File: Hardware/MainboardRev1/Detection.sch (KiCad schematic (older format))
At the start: 16 parts, among them J10 Switch_3, J11 Switch_2, J12 Switch_4, J9 Switch_1

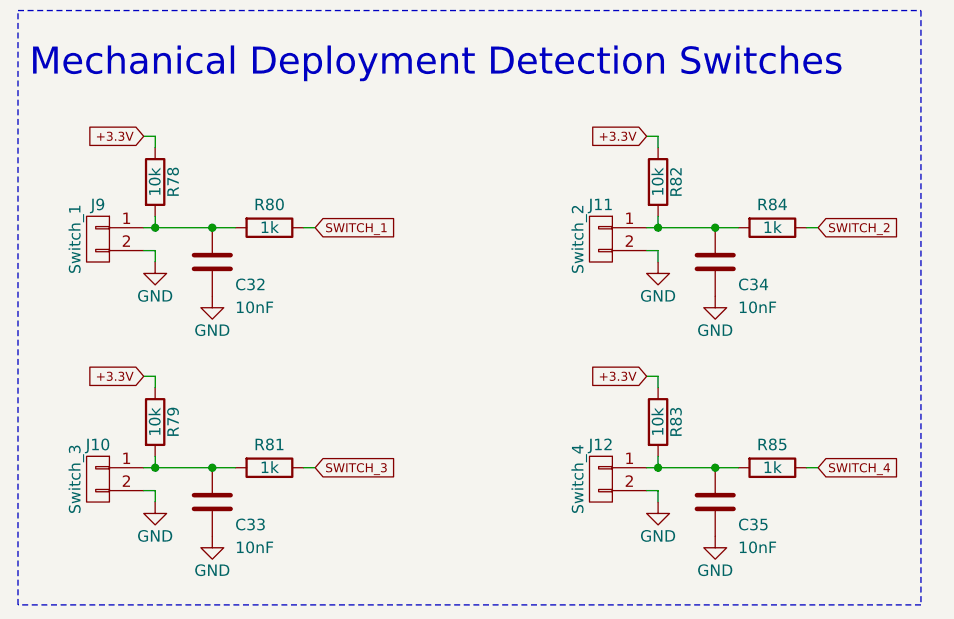
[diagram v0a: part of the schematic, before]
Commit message: Small changes to schematic: Added voltage dividers for analog inputs, small net changes. Added footprints for each part
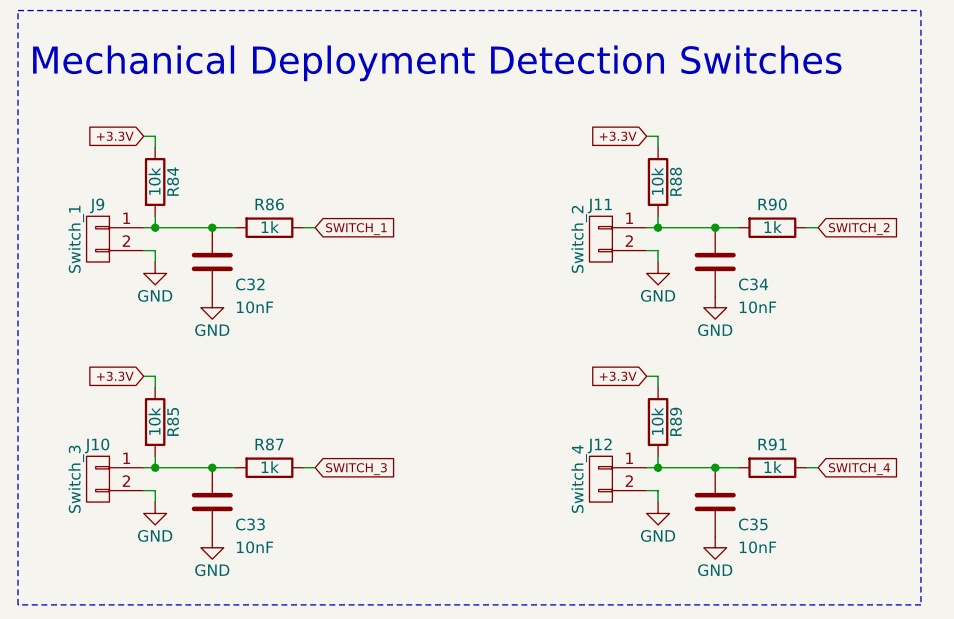
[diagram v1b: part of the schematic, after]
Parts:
- C32, C33, C34, C35: footprint (none) -> Capacitors_SMD:C_0603_HandSoldering
- J10, J11, J12, J9: footprint (none) -> Dans_Parts:Molex_Microfit3_Header_02x01_Straight
- R84: renamed from R78; footprint (none) -> Resistors_SMD:R_0603_HandSoldering
- R85: renamed from R79; footprint (none) -> Resistors_SMD:R_0603_HandSoldering
- R86: renamed from R80; footprint (none) -> Resistors_SMD:R_0603_HandSoldering
- R87: renamed from R81; footprint (none) -> Resistors_SMD:R_0603_HandSoldering
- R88: renamed from R82; footprint (none) -> Resistors_SMD:R_0603_HandSoldering
- R89: renamed from R83; footprint (none) -> Resistors_SMD:R_0603_HandSoldering
- R90: renamed from R84; footprint (none) -> Resistors_SMD:R_0603_HandSoldering
- R91: renamed from R85; footprint (none) -> Resistors_SMD:R_0603_HandSoldering
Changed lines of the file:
@@
 F 0 "J9" H 2150 2250 50  0000 C CNN
 F 1 "Switch_1" V 2250 2100 50  0000 C CNN
-F 2 "" H 2150 2100 50  0000 C CNN
+F 2 "Dans_Parts:Molex_Microfit3_Header_02x01_Straight" H 2150 2100 50  0001 C CNN
 F 3 "" H 2150 2100 50  0000 C CNN
 	1    2150 2100
@@
 $EndComp
 $Comp
-L GND #PWR070
+L GND #PWR072
 U 1 1 5AFB61FA
 P 2400 2200
-F 0 "#PWR070" H 2400 1950 50  0001 C CNN
+F 0 "#PWR072" H 2400 1950 50  0001 C CNN
 F 1 "GND" H 2400 2050 50  0000 C CNN
 F 2 "" H 2400 2200 50  0000 C CNN
@@
 	2400 2150 2350 2150
 $Comp
-L R R78
+L R R84
 U 1 1 5AFB6399
 P 2400 1850
-F 0 "R78" V 2480 1850 50  0000 C CNN
+F 0 "R84" V 2480 1850 50  0000 C CNN
 F 1 "10k" V 2400 1850 50  0000 C CNN
-F 2 "" V 2330 1850 50  0000 C CNN
+F 2 "Resistors_SMD:R_0603_HandSoldering" V 2330 1850 50  0001 C CNN
 F 3 "" H 2400 1850 50  0000 C CNN
 	1    2400 1850
@@
 F 0 "C32" H 2750 2100 50  0000 L CNN
 F 1 "10nF" H 2750 2000 50  0000 L CNN
-F 2 "" H 2688 2050 50  0000 C CNN
+F 2 "Capacitors_SMD:C_0603_HandSoldering" H 2688 2050 50  0001 C CNN
 F 3 "" H 2650 2200 50  0000 C CNN
 	1    2650 2200
@@
 	2350 2050 2750 2050
 $Comp
-L GND #PWR071
+L GND #PWR073
 U 1 1 5AFB65B1
 P 2650 2350
-F 0 "#PWR071" H 2650 2100 50  0001 C CNN
+F 0 "#PWR073" H 2650 2100 50  0001 C CNN
 F 1 "GND" H 2650 2200 50  0000 C CNN
 F 2 "" H 2650 2350 50  0000 C CNN
@@
 $EndComp
 $Comp
-L R R80
+L R R86
 U 1 1 5AFB65E3
 P 2900 2050
-F 0 "R80" V 2800 2050 50  0000 C CNN
+F 0 "R86" V 2800 2050 50  0000 C CNN
 F 1 "1k" V 2900 2050 50  0000 C CNN
-F 2 "" V 2830 2050 50  0000 C CNN
+F 2 "Resistors_SMD:R_0603_HandSoldering" V 2830 2050 50  0001 C CNN
 F 3 "" H 2900 2050 50  0000 C CNN
 	1    2900 2050
@@
 F 0 "J10" H 2150 3300 50  0000 C CNN
 F 1 "Switch_3" V 2250 3150 50  0000 C CNN
-F 2 "" H 2150 3150 50  0000 C CNN
+F 2 "Dans_Parts:Molex_Microfit3_Header_02x01_Straight" H 2150 3150 50  0001 C CNN
 F 3 "" H 2150 3150 50  0000 C CNN
 	1    2150 3150
@@
 $EndComp
 $Comp
-L GND #PWR072
+L GND #PWR074
 U 1 1 5AFB6AE1
 P 2400 3250
-F 0 "#PWR072" H 2400 3000 50  0001 C CNN
+F 0 "#PWR074" H 2400 3000 50  0001 C CNN
 F 1 "GND" H 2400 3100 50  0000 C CNN
 F 2 "" H 2400 3250 50  0000 C CNN
@@
 	2400 3200 2350 3200
 $Comp
-L R R79
+L R R85
 U 1 1 5AFB6AE9
 P 2400 2900
-F 0 "R79" V 2480 2900 50  0000 C CNN
+F 0 "R85" V 2480 2900 50  0000 C CNN
 F 1 "10k" V 2400 2900 50  0000 C CNN
-F 2 "" V 2330 2900 50  0000 C CNN
+F 2 "Resistors_SMD:R_0603_HandSoldering" V 2330 2900 50  0001 C CNN
 F 3 "" H 2400 2900 50  0000 C CNN
 	1    2400 2900
@@
 F 0 "C33" H 2750 3150 50  0000 L CNN
 F 1 "10nF" H 2750 3050 50  0000 L CNN
-F 2 "" H 2688 3100 50  0000 C CNN
+F 2 "Capacitors_SMD:C_0603_HandSoldering" H 2688 3100 50  0001 C CNN
 F 3 "" H 2650 3250 50  0000 C CNN
 	1    2650 3250
@@
 	2350 3100 2750 3100
 $Comp
-L GND #PWR073
+L GND #PWR075
 U 1 1 5AFB6AFB
 P 2650 3400
-F 0 "#PWR073" H 2650 3150 50  0001 C CNN
+F 0 "#PWR075" H 2650 3150 50  0001 C CNN
 F 1 "GND" H 2650 3250 50  0000 C CNN
 F 2 "" H 2650 3400 50  0000 C CNN
@@
 $EndComp
 $Comp
-L R R81
+L R R87
 U 1 1 5AFB6B01
 P 2900 3100
-F 0 "R81" V 2800 3100 50  0000 C CNN
+F 0 "R87" V 2800 3100 50  0000 C CNN
 F 1 "1k" V 2900 3100 50  0000 C CNN
-F 2 "" V 2830 3100 50  0000 C CNN
+F 2 "Resistors_SMD:R_0603_HandSoldering" V 2830 3100 50  0001 C CNN
 F 3 "" H 2900 3100 50  0000 C CNN
 	1    2900 3100
@@
 F 0 "J11" H 4350 2250 50  0000 C CNN
 F 1 "Switch_2" V 4450 2100 50  0000 C CNN
-F 2 "" H 4350 2100 50  0000 C CNN
+F 2 "Dans_Parts:Molex_Microfit3_Header_02x01_Straight" H 4350 2100 50  0001 C CNN
 F 3 "" H 4350 2100 50  0000 C CNN
 	1    4350 2100
@@
 $EndComp
 $Comp
-L GND #PWR074
+L GND #PWR076
 U 1 1 5AFB6C68
 P 4600 2200
-F 0 "#PWR074" H 4600 1950 50  0001 C CNN
+F 0 "#PWR076" H 4600 1950 50  0001 C CNN
 F 1 "GND" H 4600 2050 50  0000 C CNN
 F 2 "" H 4600 2200 50  0000 C CNN
@@
 	4600 2150 4550 2150
 $Comp
-L R R82
+L R R88
 U 1 1 5AFB6C70
 P 4600 1850
-F 0 "R82" V 4680 1850 50  0000 C CNN
+F 0 "R88" V 4680 1850 50  0000 C CNN
 F 1 "10k" V 4600 1850 50  0000 C CNN
-F 2 "" V 4530 1850 50  0000 C CNN
+F 2 "Resistors_SMD:R_0603_HandSoldering" V 4530 1850 50  0001 C CNN
 F 3 "" H 4600 1850 50  0000 C CNN
 	1    4600 1850
@@
 F 0 "C34" H 4950 2100 50  0000 L CNN
 F 1 "10nF" H 4950 2000 50  0000 L CNN
-F 2 "" H 4888 2050 50  0000 C CNN
+F 2 "Capacitors_SMD:C_0603_HandSoldering" H 4888 2050 50  0001 C CNN
 F 3 "" H 4850 2200 50  0000 C CNN
 	1    4850 2200
@@
 	4550 2050 4950 2050
 $Comp
-L GND #PWR075
+L GND #PWR077
 U 1 1 5AFB6C82
 P 4850 2350
-F 0 "#PWR075" H 4850 2100 50  0001 C CNN
+F 0 "#PWR077" H 4850 2100 50  0001 C CNN
 F 1 "GND" H 4850 2200 50  0000 C CNN
 F 2 "" H 4850 2350 50  0000 C CNN
@@
 $EndComp
 $Comp
-L R R84
+L R R90
 U 1 1 5AFB6C88
 P 5100 2050
-F 0 "R84" V 5000 2050 50  0000 C CNN
+F 0 "R90" V 5000 2050 50  0000 C CNN
 F 1 "1k" V 5100 2050 50  0000 C CNN
-F 2 "" V 5030 2050 50  0000 C CNN
+F 2 "Resistors_SMD:R_0603_HandSoldering" V 5030 2050 50  0001 C CNN
 F 3 "" H 5100 2050 50  0000 C CNN
 	1    5100 2050
@@
 F 0 "J12" H 4350 3300 50  0000 C CNN
 F 1 "Switch_4" V 4450 3150 50  0000 C CNN
-F 2 "" H 4350 3150 50  0000 C CNN
+F 2 "Dans_Parts:Molex_Microfit3_Header_02x01_Straight" H 4350 3150 50  0001 C CNN
 F 3 "" H 4350 3150 50  0000 C CNN
 	1    4350 3150
@@
 $EndComp
 $Comp
-L GND #PWR076
+L GND #PWR078
 U 1 1 5AFB6C97
 P 4600 3250
-F 0 "#PWR076" H 4600 3000 50  0001 C CNN
+F 0 "#PWR078" H 4600 3000 50  0001 C CNN
 F 1 "GND" H 4600 3100 50  0000 C CNN
 F 2 "" H 4600 3250 50  0000 C CNN
@@
 	4600 3200 4550 3200
 $Comp
-L R R83
+L R R89
 U 1 1 5AFB6C9F
 P 4600 2900
-F 0 "R83" V 4680 2900 50  0000 C CNN
+F 0 "R89" V 4680 2900 50  0000 C CNN
 F 1 "10k" V 4600 2900 50  0000 C CNN
-F 2 "" V 4530 2900 50  0000 C CNN
+F 2 "Resistors_SMD:R_0603_HandSoldering" V 4530 2900 50  0001 C CNN
 F 3 "" H 4600 2900 50  0000 C CNN
 	1    4600 2900
@@
 F 0 "C35" H 4950 3150 50  0000 L CNN
 F 1 "10nF" H 4950 3050 50  0000 L CNN
-F 2 "" H 4888 3100 50  0000 C CNN
+F 2 "Capacitors_SMD:C_0603_HandSoldering" H 4888 3100 50  0001 C CNN
 F 3 "" H 4850 3250 50  0000 C CNN
 	1    4850 3250
@@
 	4550 3100 4950 3100
 $Comp
-L GND #PWR077
+L GND #PWR079
 U 1 1 5AFB6CB1
 P 4850 3400
-F 0 "#PWR077" H 4850 3150 50  0001 C CNN
+F 0 "#PWR079" H 4850 3150 50  0001 C CNN
 F 1 "GND" H 4850 3250 50  0000 C CNN
 F 2 "" H 4850 3400 50  0000 C CNN
@@
 $EndComp
 $Comp
-L R R85
+L R R91
 U 1 1 5AFB6CB7
 P 5100 3100
-F 0 "R85" V 5000 3100 50  0000 C CNN
+F 0 "R91" V 5000 3100 50  0000 C CNN
 F 1 "1k" V 5100 3100 50  0000 C CNN
-F 2 "" V 5030 3100 50  0000 C CNN
+F 2 "Resistors_SMD:R_0603_HandSoldering" V 5030 3100 50  0001 C CNN
 F 3 "" H 5100 3100 50  0000 C CNN
 	1    5100 3100

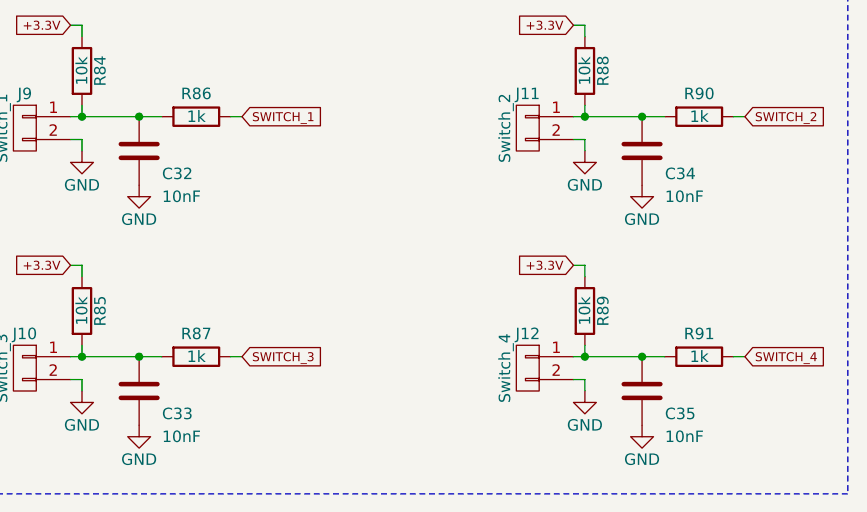
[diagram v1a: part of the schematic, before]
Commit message: Components placed. Needs to be routed.
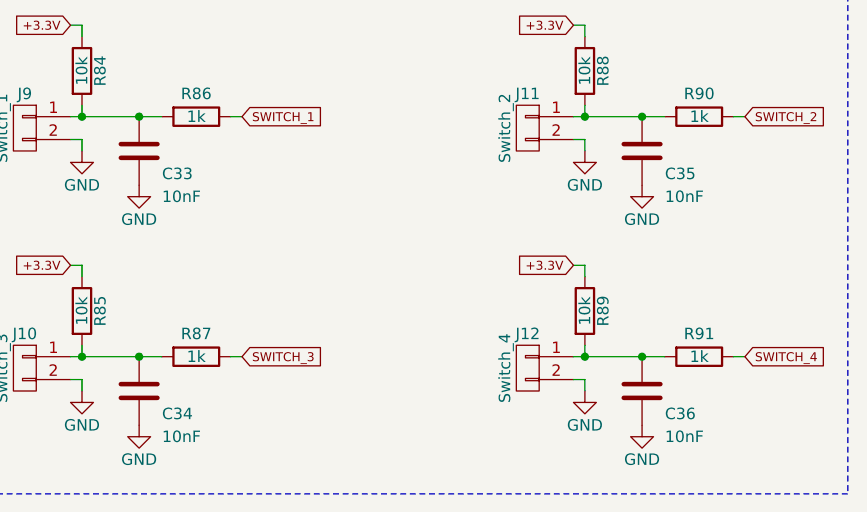
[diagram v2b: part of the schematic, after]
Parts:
- J10, J11, J12, J9: footprint Dans_Parts:Molex_Microfit3_Header_02x01_Straight -> Dans_Parts:CONN_2POS_VERT_TE_CONN_LOCK_5-103669-1
- renumbered C32 to C33, C33 to C34, C34 to C35, C35 to C36
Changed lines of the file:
@@
 LIBS:teensy3_6-OuterHeadersOnly
 LIBS:switches
+LIBS:mounting_hole_eighth_inch
 LIBS:MainboardRev1-cache
 EELAYER 25 0
@@
 F 0 "J9" H 2150 2250 50  0000 C CNN
 F 1 "Switch_1" V 2250 2100 50  0000 C CNN
-F 2 "Dans_Parts:Molex_Microfit3_Header_02x01_Straight" H 2150 2100 50  0001 C CNN
+F 2 "Dans_Parts:CONN_2POS_VERT_TE_CONN_LOCK_5-103669-1" H 2150 2100 50  0001 C CNN
 F 3 "" H 2150 2100 50  0000 C CNN
 	1    2150 2100
@@
 $EndComp
 $Comp
-L GND #PWR072
+L GND #PWR078
 U 1 1 5AFB61FA
 P 2400 2200
-F 0 "#PWR072" H 2400 1950 50  0001 C CNN
+F 0 "#PWR078" H 2400 1950 50  0001 C CNN
 F 1 "GND" H 2400 2050 50  0000 C CNN
 F 2 "" H 2400 2200 50  0000 C CNN
@@
 Connection ~ 2400 2050
 $Comp
-L C C32
+L C C33
 U 1 1 5AFB656E
 P 2650 2200
-F 0 "C32" H 2750 2100 50  0000 L CNN
+F 0 "C33" H 2750 2100 50  0000 L CNN
 F 1 "10nF" H 2750 2000 50  0000 L CNN
 F 2 "Capacitors_SMD:C_0603_HandSoldering" H 2688 2050 50  0001 C CNN
@@
 	2350 2050 2750 2050
 $Comp
-L GND #PWR073
+L GND #PWR079
 U 1 1 5AFB65B1
 P 2650 2350
-F 0 "#PWR073" H 2650 2100 50  0001 C CNN
+F 0 "#PWR079" H 2650 2100 50  0001 C CNN
 F 1 "GND" H 2650 2200 50  0000 C CNN
 F 2 "" H 2650 2350 50  0000 C CNN
@@
 F 0 "J10" H 2150 3300 50  0000 C CNN
 F 1 "Switch_3" V 2250 3150 50  0000 C CNN
-F 2 "Dans_Parts:Molex_Microfit3_Header_02x01_Straight" H 2150 3150 50  0001 C CNN
+F 2 "Dans_Parts:CONN_2POS_VERT_TE_CONN_LOCK_5-103669-1" H 2150 3150 50  0001 C CNN
 F 3 "" H 2150 3150 50  0000 C CNN
 	1    2150 3150
@@
 $EndComp
 $Comp
-L GND #PWR074
+L GND #PWR080
 U 1 1 5AFB6AE1
 P 2400 3250
-F 0 "#PWR074" H 2400 3000 50  0001 C CNN
+F 0 "#PWR080" H 2400 3000 50  0001 C CNN
 F 1 "GND" H 2400 3100 50  0000 C CNN
 F 2 "" H 2400 3250 50  0000 C CNN
@@
 Connection ~ 2400 3100
 $Comp
-L C C33
+L C C34
 U 1 1 5AFB6AF4
 P 2650 3250
-F 0 "C33" H 2750 3150 50  0000 L CNN
+F 0 "C34" H 2750 3150 50  0000 L CNN
 F 1 "10nF" H 2750 3050 50  0000 L CNN
 F 2 "Capacitors_SMD:C_0603_HandSoldering" H 2688 3100 50  0001 C CNN
@@
 	2350 3100 2750 3100
 $Comp
-L GND #PWR075
+L GND #PWR081
 U 1 1 5AFB6AFB
 P 2650 3400
-F 0 "#PWR075" H 2650 3150 50  0001 C CNN
+F 0 "#PWR081" H 2650 3150 50  0001 C CNN
 F 1 "GND" H 2650 3250 50  0000 C CNN
 F 2 "" H 2650 3400 50  0000 C CNN
@@
 F 0 "J11" H 4350 2250 50  0000 C CNN
 F 1 "Switch_2" V 4450 2100 50  0000 C CNN
-F 2 "Dans_Parts:Molex_Microfit3_Header_02x01_Straight" H 4350 2100 50  0001 C CNN
+F 2 "Dans_Parts:CONN_2POS_VERT_TE_CONN_LOCK_5-103669-1" H 4350 2100 50  0001 C CNN
 F 3 "" H 4350 2100 50  0000 C CNN
 	1    4350 2100
@@
 $EndComp
 $Comp
-L GND #PWR076
+L GND #PWR082
 U 1 1 5AFB6C68
 P 4600 2200
-F 0 "#PWR076" H 4600 1950 50  0001 C CNN
+F 0 "#PWR082" H 4600 1950 50  0001 C CNN
 F 1 "GND" H 4600 2050 50  0000 C CNN
 F 2 "" H 4600 2200 50  0000 C CNN
@@
 Connection ~ 4600 2050
 $Comp
-L C C34
+L C C35
 U 1 1 5AFB6C7B
 P 4850 2200
-F 0 "C34" H 4950 2100 50  0000 L CNN
+F 0 "C35" H 4950 2100 50  0000 L CNN
 F 1 "10nF" H 4950 2000 50  0000 L CNN
 F 2 "Capacitors_SMD:C_0603_HandSoldering" H 4888 2050 50  0001 C CNN
@@
 	4550 2050 4950 2050
 $Comp
-L GND #PWR077
+L GND #PWR083
 U 1 1 5AFB6C82
 P 4850 2350
-F 0 "#PWR077" H 4850 2100 50  0001 C CNN
+F 0 "#PWR083" H 4850 2100 50  0001 C CNN
 F 1 "GND" H 4850 2200 50  0000 C CNN
 F 2 "" H 4850 2350 50  0000 C CNN
@@
 F 0 "J12" H 4350 3300 50  0000 C CNN
 F 1 "Switch_4" V 4450 3150 50  0000 C CNN
-F 2 "Dans_Parts:Molex_Microfit3_Header_02x01_Straight" H 4350 3150 50  0001 C CNN
+F 2 "Dans_Parts:CONN_2POS_VERT_TE_CONN_LOCK_5-103669-1" H 4350 3150 50  0001 C CNN
 F 3 "" H 4350 3150 50  0000 C CNN
 	1    4350 3150
@@
 $EndComp
 $Comp
-L GND #PWR078
+L GND #PWR084
 U 1 1 5AFB6C97
 P 4600 3250
-F 0 "#PWR078" H 4600 3000 50  0001 C CNN
+F 0 "#PWR084" H 4600 3000 50  0001 C CNN
 F 1 "GND" H 4600 3100 50  0000 C CNN
 F 2 "" H 4600 3250 50  0000 C CNN
@@
 Connection ~ 4600 3100
 $Comp
-L C C35
+L C C36
 U 1 1 5AFB6CAA
 P 4850 3250
-F 0 "C35" H 4950 3150 50  0000 L CNN
+F 0 "C36" H 4950 3150 50  0000 L CNN
 F 1 "10nF" H 4950 3050 50  0000 L CNN
 F 2 "Capacitors_SMD:C_0603_HandSoldering" H 4888 3100 50  0001 C CNN
@@
 	4550 3100 4950 3100
 $Comp
-L GND #PWR079
+L GND #PWR085
 U 1 1 5AFB6CB1
 P 4850 3400
-F 0 "#PWR079" H 4850 3150 50  0001 C CNN
+F 0 "#PWR085" H 4850 3150 50  0001 C CNN
 F 1 "GND" H 4850 3250 50  0000 C CNN
 F 2 "" H 4850 3400 50  0000 C CNN
